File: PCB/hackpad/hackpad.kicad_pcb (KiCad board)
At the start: 2 copper layers, 63.5 x 66 mm, 9 parts, among them J1 Conn_01x04, SW1 SW_Push, SW2 SW_Push, SW3 SW_Push, SW4 SW_Push, SW5 SW_Push, SW6 SW_Push, SW7 RotaryEncoder_Switch, U1 XIAO-RP2040-DIP

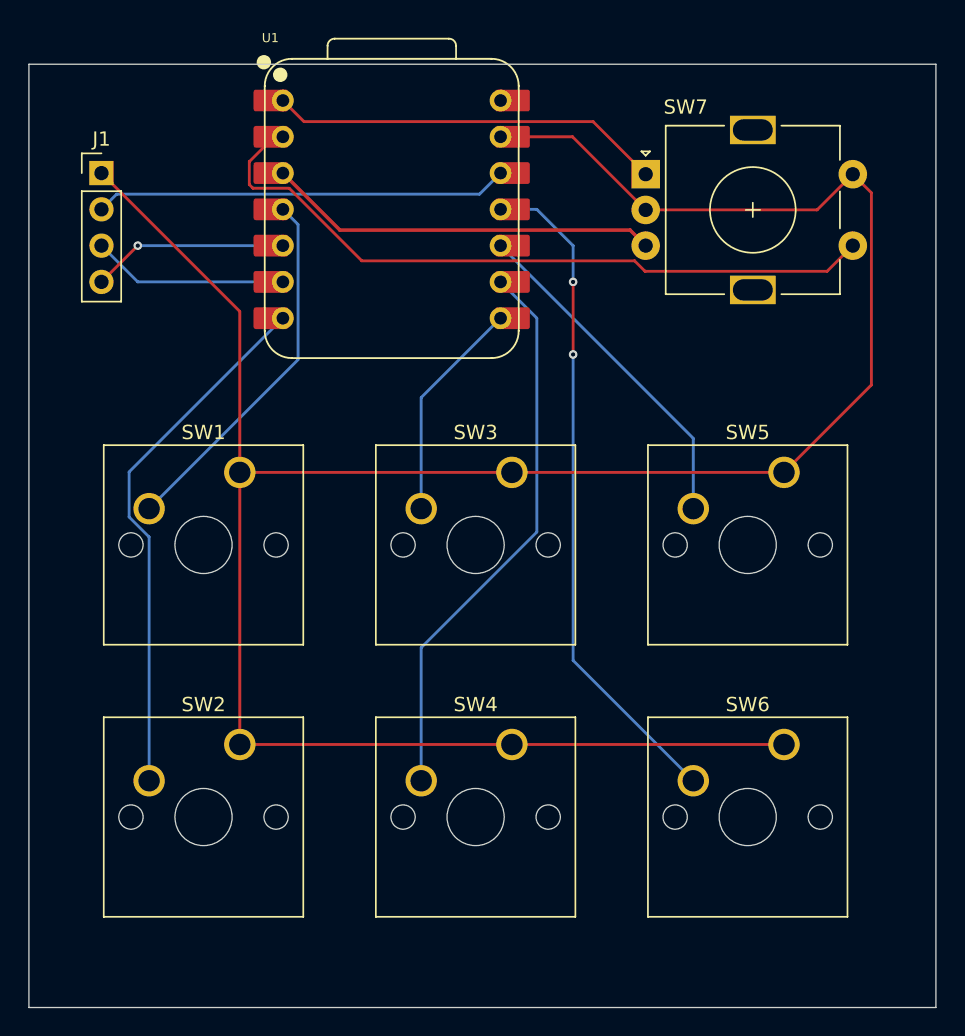
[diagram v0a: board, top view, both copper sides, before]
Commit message: Moved XIAO Microcontroller to back
This change was made to avoid any physical overlap with the 1inch OLED display
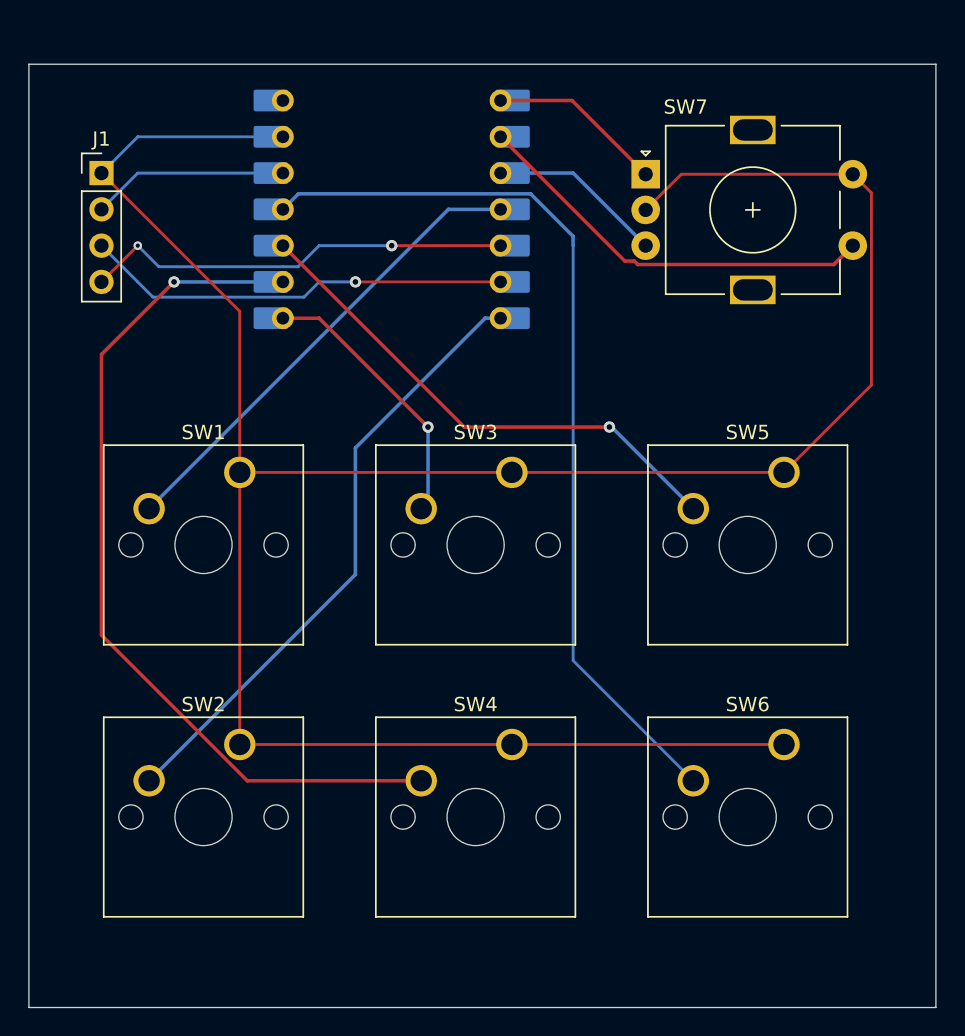
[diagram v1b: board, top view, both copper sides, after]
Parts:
- U1: moved to B.Cu
- turned U1 to 180 degrees
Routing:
- net Net-(U1-GPIO2/SCK): track 39.3 -> 61.1 mm, vias 0 -> 1
- net Net-(U1-GPIO27/ADC1/A1): track 50.2 -> 28.9 mm
- net Net-(U1-GPIO28/ADC2/A2): track 29.0 -> 11.4 mm
- net Net-(U1-GPIO3/MOSI): track 47.1 -> 63.6 mm, vias 2 -> 0
- net Net-(J1-Pin_4): track 13.8 -> 30.2 mm, vias 1 -> 2
- net Net-(J1-Pin_3): track 13.8 -> 29.9 mm, vias 0 -> 1
- net Net-(U1-GPIO26/ADC0/A0): track 27.5 -> 12.3 mm
- net Net-(J1-Pin_2): track 29.0 -> 13.8 mm
- net Net-(U1-GPIO4/MISO): track 24.0 -> 36.4 mm, vias 0 -> 1
- net Net-(U1-GPIO29/ADC3/A3): track 25.7 -> 33.3 mm
- net Net-(U1-GPIO0/TX): track 37.4 -> 43.2 mm
- net Net-(U1-GPIO1/RX): track 15.6 -> 19.2 mm, vias 0 -> 1
- net Net-(J1-Pin_1): track 172.0 -> 174.1 mm

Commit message: Added branding to board
+Cleaned up a few connections
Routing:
- net Net-(J1-Pin_4): track 30.2 -> 29.0 mm
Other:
- board text added: "Chester's Hackpad"
- board text added: "XIAO HERE"
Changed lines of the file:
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@@
 		(layer "Edge.Cuts")
+	)
+	(gr_text "Chester's Hackpad"
+		(at 72.136 111.76 0)
+		(layer "F.SilkS")
+		(effects
+			(font
+				(size 1 1)
+				(thickness 0.1)
+			)
+			(justify left bottom)
+		)
+	)
+	(gr_text "XIAO HERE"
+		(at 101.6 116.84 0)
+		(layer "B.SilkS")
+		(effects
+			(font
+				(size 1 1)
+				(thickness 0.1)
+			)
+			(justify left bottom mirror)
+		)
 	)
 	(segment
@@
 	)
 	(segment
+		(start 88.9 114.3)
+		(end 87.884 114.3)
+		(width 0.25)
+		(layer "F.Cu")
+		(net 11)
+	)
+	(segment
 		(start 123.98375 137.795)
 		(end 85.88375 137.795)
@@
 	)
 	(segment
+		(start 87.884 114.3)
+		(end 85.344 116.84)
+		(width 0.25)
+		(layer "F.Cu")
+		(net 11)
+	)
+	(segment
 		(start 85.88375 126.52375)
 		(end 76.2 116.84)
@@
 	)
 	(segment
-		(start 78.74 114.3)
-		(end 88.9 114.3)
-		(width 0.2)
-		(layer "B.Cu")
-		(net 11)
-	)
-	(segment
-		(start 76.2 116.84)
-		(end 78.74 114.3)
-		(width 0.2)
-		(layer "B.Cu")
-		(net 11)
+		(start 85.344 116.84)
+		(end 76.2 116.84)
+		(width 0.25)
+		(layer "F.Cu")
+		(net 11)
+	)
+	(segment
+		(start 77.263 123.397)
+		(end 80.217 123.397)
+		(width 0.2)
+		(layer "F.Cu")
+		(net 12)
+	)
+	(segment
+		(start 76.2 124.46)
+		(end 77.263 123.397)
+		(width 0.2)
+		(layer "F.Cu")
+		(net 12)
 	)
 	(segment
 		(start 96.52 121.92)
 		(end 104.14 121.92)
-		(width 0.2)
-		(layer "F.Cu")
-		(net 12)
-	)
-	(segment
-		(start 76.2 124.46)
-		(end 78.74 121.92)
 		(width 0.2)
 		(layer "F.Cu")
@@
 	)
 	(via
-		(at 78.74 121.92)
+		(at 80.217 123.397)
 		(size 0.6)
 		(drill 0.3)
@@
 	)
 	(segment
+		(start 80.217 123.397)
+		(end 89.963 123.397)
+		(width 0.2)
+		(layer "B.Cu")
+		(net 12)
+	)
+	(segment
 		(start 89.963 123.397)
 		(end 91.44 121.92)
 		(width 0.2)
 		(layer "B.Cu")
-		(net 12)
-	)
-	(segment
-		(start 80.217 123.397)
-		(end 88.9 123.397)
-		(width 0.2)
-		(layer "B.Cu")
-		(net 12)
-	)
-	(segment
-		(start 78.74 121.92)
-		(end 80.217 123.397)
-		(width 0.2)
-		(layer "B.Cu")
-		(net 12)
-	)
-	(segment
-		(start 88.9 123.397)
-		(end 89.963 123.397)
-		(width 0.2)
-		(layer "B.Cu")
